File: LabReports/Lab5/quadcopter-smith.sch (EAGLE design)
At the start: 58 parts, among them J1 AVR_SPI_PRG_6NS, Q1 SI2302CDS, Q2 SI2302CDS, Q3 SI2302CDS, Q4 SI2302CDS, U1 ATMEGA128RFA1, U2 LSM9DS0-LGA24, Y1 16MHz

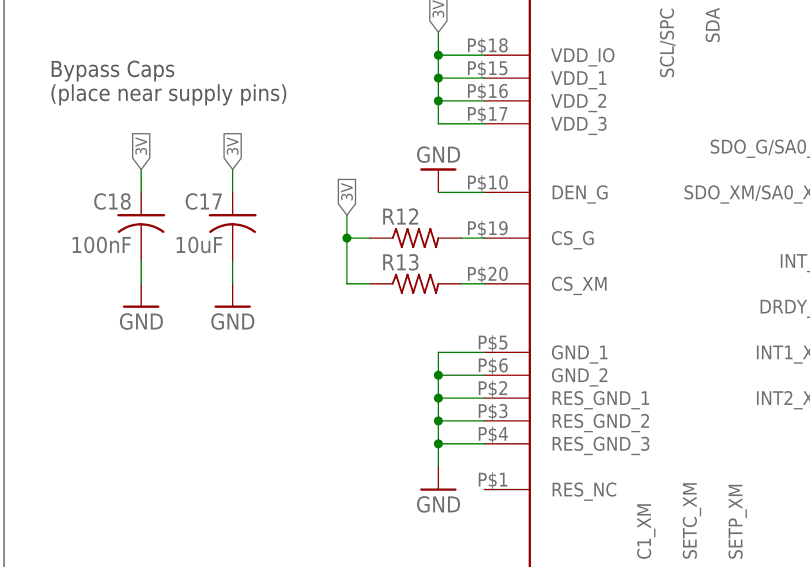
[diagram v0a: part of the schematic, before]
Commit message: Binged on manual routing
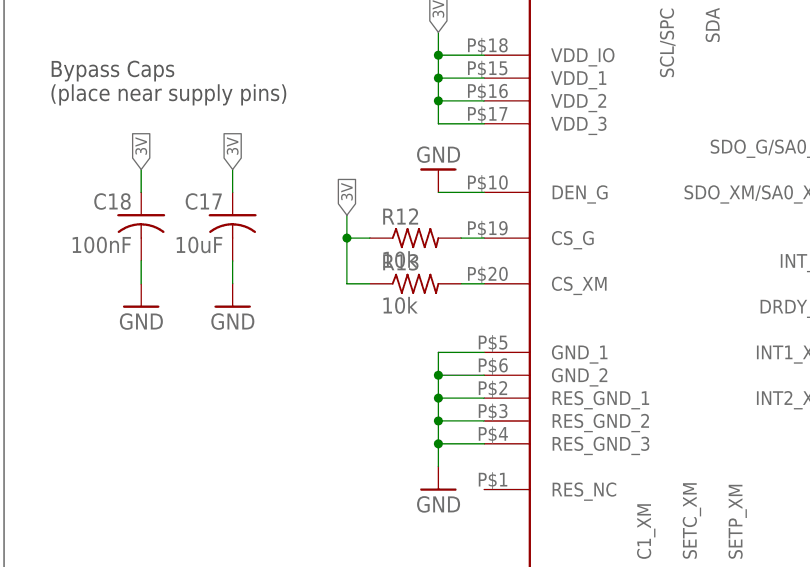
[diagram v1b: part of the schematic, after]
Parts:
- R12, R13: value (none) -> 10k
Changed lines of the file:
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@@
 <part name="GND36" library="Lab5" deviceset="GND" device=""/>
 <part name="GND37" library="Lab5" deviceset="GND" device=""/>
-<part name="R12" library="Lab5" deviceset="R-US_" device="R0805"/>
-<part name="R13" library="Lab5" deviceset="R-US_" device="R0805"/>
+<part name="R12" library="Lab5" deviceset="R-US_" device="R0805" value="10k"/>
+<part name="R13" library="Lab5" deviceset="R-US_" device="R0805" value="10k"/>
 </parts>
 <sheets>
